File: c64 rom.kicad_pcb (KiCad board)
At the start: 2 copper layers, 22 x 41 mm, 6 parts, among them U1 27C256

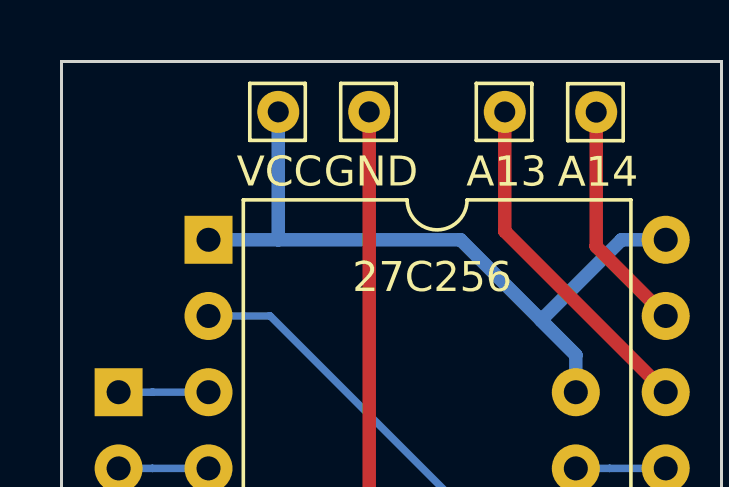
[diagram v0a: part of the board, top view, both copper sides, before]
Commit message: Main: Fix Incorrect naming of 5V terminal
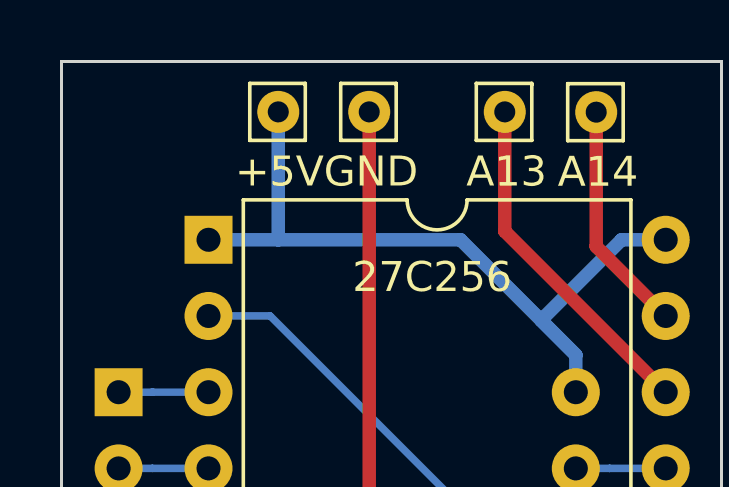
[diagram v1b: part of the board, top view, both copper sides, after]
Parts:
- VCC1: value VCC -> +5V
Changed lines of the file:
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@@
         (effects (font (size 1 1) (thickness 0.15)))
     )
-    (fp_text value "VCC" (at 0.039618 1.991157) (layer "F.SilkS")
+    (fp_text value "+5V" (at 0.039618 1.991157) (layer "F.SilkS")
         (effects (font (size 1 1) (thickness 0.15)))
     )
